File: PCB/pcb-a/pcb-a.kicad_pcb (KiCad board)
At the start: 2 copper layers, 94.9 x 43.5 mm, 24 parts, among them J1 Conn_02x05_Counter_Clockwise, J2 Conn_02x05_Counter_Clockwise, Q3 BC337, SW1 config, U1 ESP32-S2-DevKitM, U3 L7805

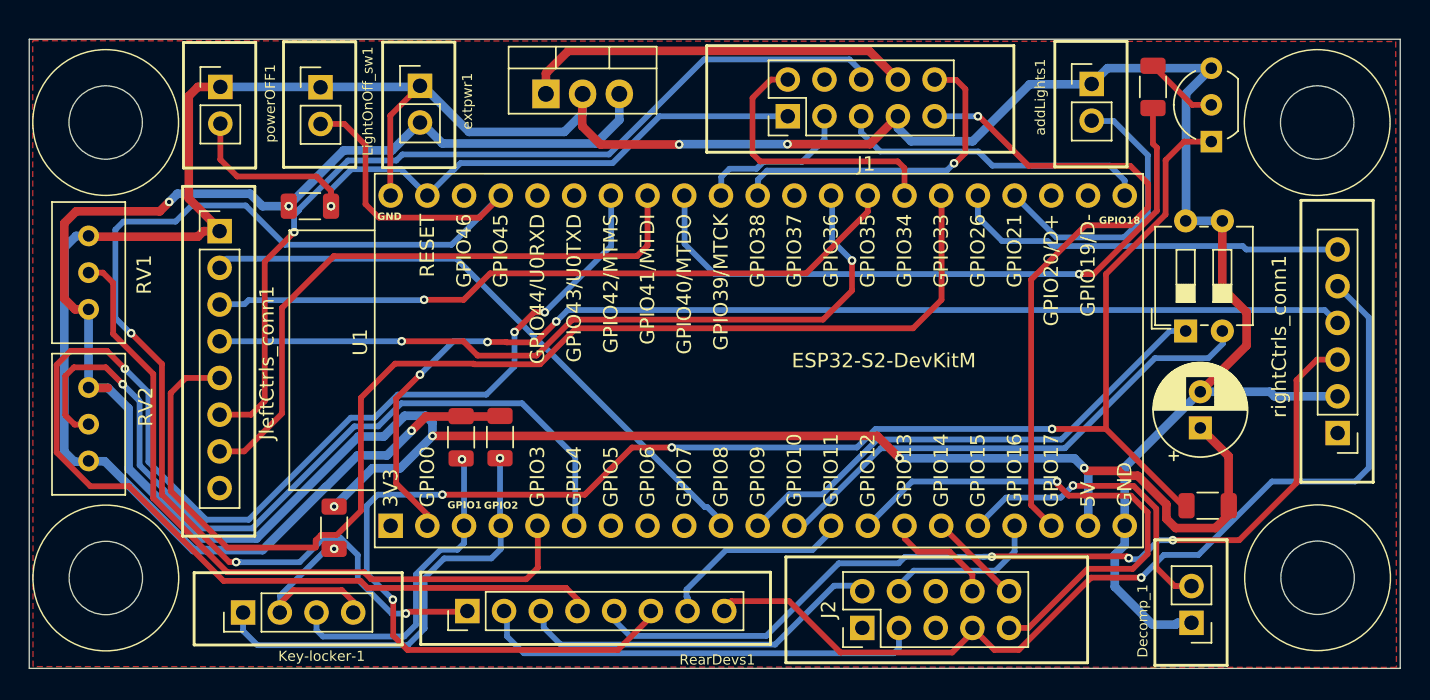
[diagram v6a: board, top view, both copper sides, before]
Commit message: Communication with the rear power stage has been changed
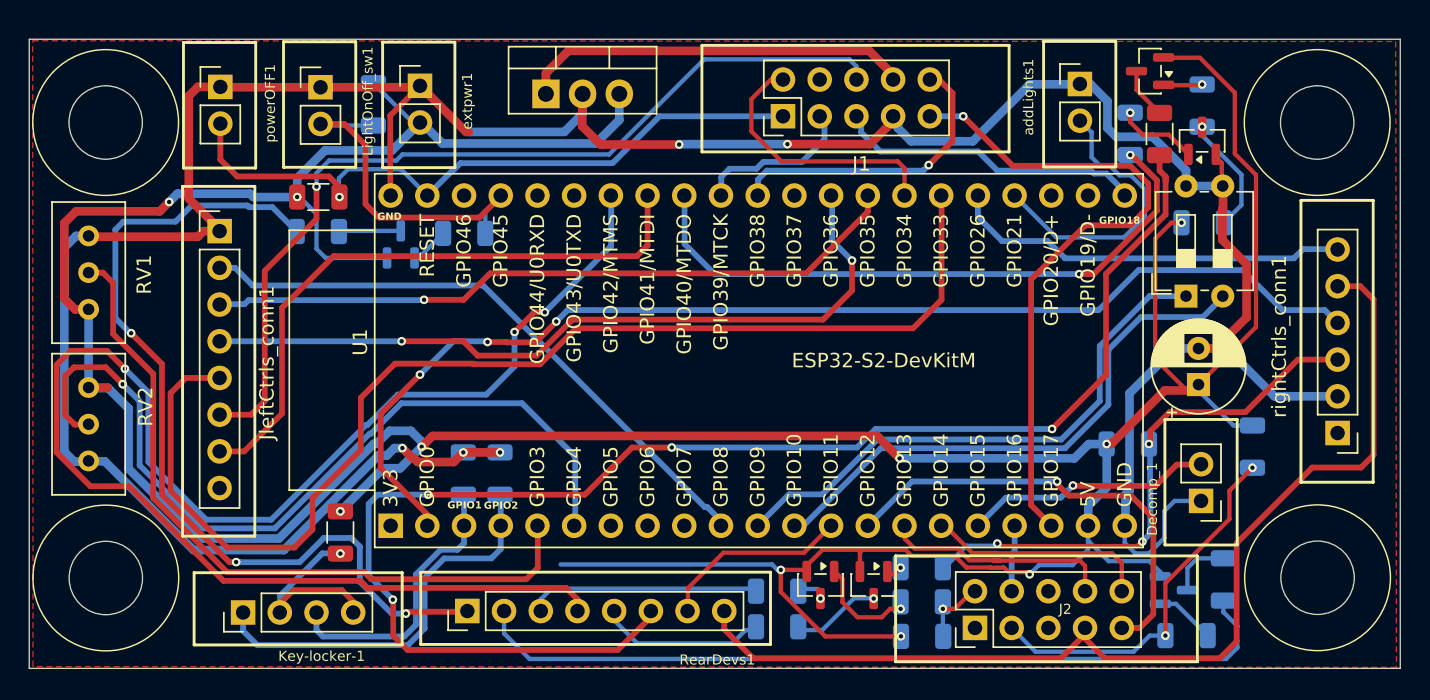
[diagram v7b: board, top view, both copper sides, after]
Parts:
- added Q1: BC807, Package_TO_SOT_SMD:SOT-23, F.Cu at (187.1, 63.9)
- added Q2: BC807, Package_TO_SOT_SMD:SOT-23, F.Cu at (164.3, 99.4)
- added Q4: BC807, Package_TO_SOT_SMD:SOT-23, B.Cu at (188.7, 99.8)
- added Q5: BC807, Package_TO_SOT_SMD:SOT-23, F.Cu at (168.0, 99.4)
- added Q6: BC807, Package_TO_SOT_SMD:SOT-23, B.Cu at (135.2, 75.9)
- added R10: 10K, Resistor_SMD:R_1206_3216Metric, B.Cu at (190.7, 66.3)
- added R11: 1K, Resistor_SMD:R_1206_3216Metric, B.Cu at (192.2, 99.0)
- added R12: 1K, Resistor_SMD:R_1206_3216Metric, B.Cu at (161.3, 99.9)
- added R13: 1K, Resistor_SMD:R_1206_3216Metric, B.Cu at (161.3, 102.3)
- added R14: 100K, Resistor_SMD:R_1206_3216Metric, B.Cu at (185.5, 89.7)
- added R15: 1K, Resistor_SMD:R_1206_3216Metric, F.Cu at (187.7, 68.2)
- added R16: 100K, Resistor_SMD:R_1206_3216Metric, B.Cu at (171.3, 103.0)
- added R17: 100K, Resistor_SMD:R_1206_3216Metric, B.Cu at (194.2, 89.9)
- added R18: 10K, Resistor_SMD:R_1206_3216Metric, B.Cu at (139.6, 75.1)
- added R19: 100K, Resistor_SMD:R_1206_3216Metric, B.Cu at (133.3, 66.2)
- added R20: 1K, Resistor_SMD:R_1206_3216Metric, B.Cu at (129.5, 75.0)
- added R5: 10K, Resistor_SMD:R_1206_3216Metric, B.Cu at (171.3, 100.6)
- added R8: 10K, Resistor_SMD:R_1206_3216Metric, B.Cu at (189.6, 102.9)
- added R9: 10K, Resistor_SMD:R_1206_3216Metric, B.Cu at (171.3, 98.2)
- Q3: value BC337 -> BC817; footprint Package_TO_SOT_THT:TO-92_Inline_Wide -> Package_TO_SOT_SMD:SOT-23
- R3, R4, R6, R7: moved to B.Cu
- moved R6 19.6 mm to (190.7, 74.4), turned to 180 degrees
- moved Decomp_1 8.46 mm to (190.6, 93.6)
- moved J2 7.80 mm to (175.0, 102.4)
- moved R7 3.61 mm to (185.7, 68.2)
- moved C1 3.00 mm to (190.4, 85.6)
- moved R4 2.53 mm to (142.1, 91.7)
- moved R3 2.52 mm to (139.6, 91.7)
- moved SW1 2.41 mm to (189.6, 79.4)
- moved R2 0.86 mm to (129.5, 72.6)
- moved addLights1 0.81 mm to (182.2, 64.8)
- moved Q3 0.64 mm to (190.7, 68.7)
- moved R1 0.54 mm to (131.0, 95.8)
- moved J1 0.33 mm to (161.7, 67.0)
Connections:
- J2 pad 2: c_rightArrow -> Net-(J2-Pin_2)
- J2 pad 3: c_leftArrow -> Net-(J2-Pin_3)
- LightOnOff_sw1 pad 2: c_rearLight -> i_lightON/OFF
- Q3 pad 1: c_startEngine -> Net-(Q3-B)
- Q3 pad 2: Net-(Q3-B) -> GND
- Q3 pad 3: GND -> Net-(Q3-C)
- R6 pad 1: c_startEngine -> Net-(Q3-C)
- U1 pad 39: c_rearLight -> i_lightON/OFF
- rightCtrls_conn1 pad 3: c_brakeSwitch -> Net-(rightCtrls_conn1-Pin_3)
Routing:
- net 5V: track 172.8 -> 286.0 mm, vias 6 -> 10
- net c_brakeSwitch: track 63.5 -> 11.6 mm, vias 3 -> 0
- net Net-(rightCtrls_conn1-Pin_3): track 0.00 -> 37.7 mm, vias 0 -> 3
- net c_rearLight: track 94.9 -> 61.1 mm
- net c_leftArrow: track 31.0 -> 57.1 mm
- net Net-(J2-Pin_3): track 0.00 -> 25.9 mm, vias 0 -> 2
- net i_lightON/OFF: track 0.00 -> 25.0 mm
- net c_startEngine: track 114.5 -> 101.6 mm
- net o_neutral: track 6.55 -> 15.5 mm
- net c_rightArrow: track 25.6 -> 16.7 mm
- net Net-(Q3-C): track 0.00 -> 8.23 mm, vias 0 -> 1
- net o_engineReady: track 7.77 -> 15.9 mm
- net Net-(Q2-B): track 0.00 -> 7.09 mm, vias 0 -> 1
- net o_engineON: track 11.2 -> 4.62 mm
- net c_engineOFF: track 66.7 -> 73.1 mm, vias 1 -> 0
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
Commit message: Small enhancements
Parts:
- moved R2 0.43 mm to (129.1, 72.6)
- moved R20 0.42 mm to (129.1, 75.0)
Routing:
- net o_startEngine: track 43.0 -> 44.6 mm
- net c_engineOFF: track 73.1 -> 72.5 mm, vias 0 -> 1
- net i_rightArrow: vias 0 -> 2
